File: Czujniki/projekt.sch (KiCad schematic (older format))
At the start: 44 parts, among them P1 CONN_01X08, U1 MCP1700, U10 PCA9306, U12 SHTC1, U14 LM4041, U15 MCP6231, U6 MCP3201, U7 DS1338, U8 MCP6L1, U9 MCP6L1, Y1 Crystal

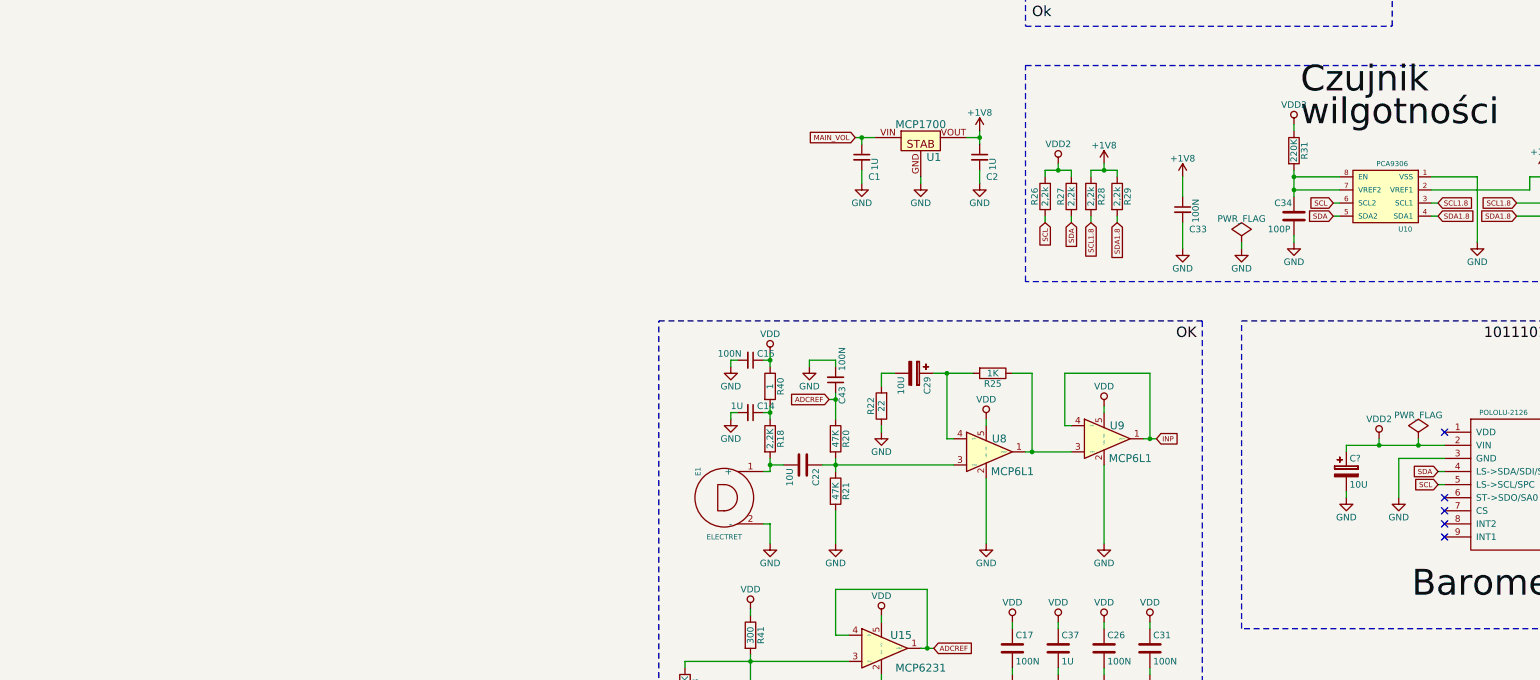
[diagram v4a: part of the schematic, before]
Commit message: Edits + additional program for dust controller
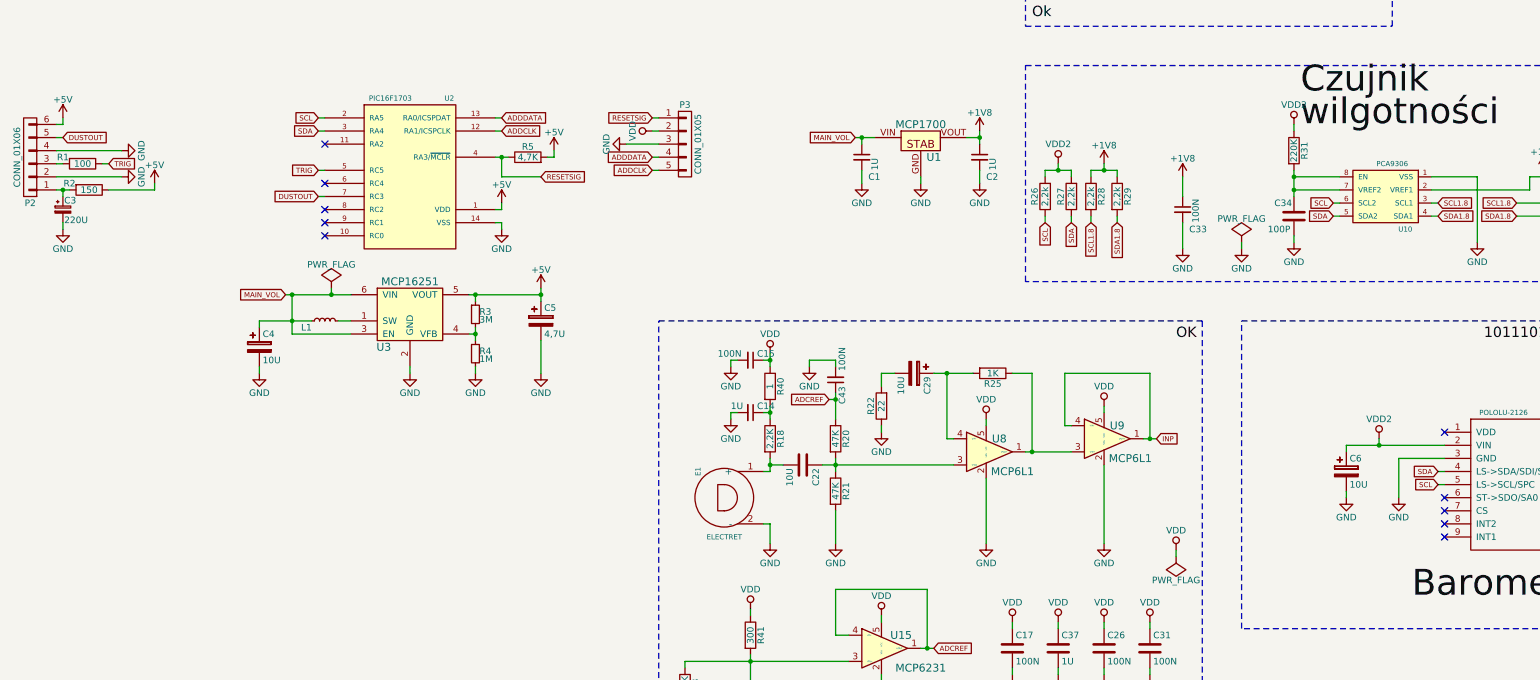
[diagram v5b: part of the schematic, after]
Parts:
- added C3: 220U, Capacitors_Tantalum_SMD:TantalC_SizeX_EIA-7343, symbol CP_Small
- added C4: 10U, Capacitors_Tantalum_SMD:TantalC_SizeX_EIA-7343, symbol CP
- added C5: 4,7U, Capacitors_Tantalum_SMD:TantalC_SizeA_EIA-3216_HandSoldering, symbol CP
- added L1: NLCV32T-4R7M-PF, SMD_Packages:SMD-1210_Pol, symbol L_Small
- added P2: CONN_01X06, Socket_Strips:Socket_Strip_Straight_1x06, symbol CONN_01X06
- added P3: CONN_01X05, Socket_Strips:Socket_Strip_Straight_1x05, symbol CONN_01X05
- added R1: 100, Resistors_SMD:R_0603, symbol R
- added R2: 150, Resistors_SMD:R_0805, symbol R
- added R3: 3M, Resistors_SMD:R_0603, symbol R_Small
- added R4: 1M, Resistors_SMD:R_0603, symbol R_Small
- added R5: 4,7K, Resistors_SMD:R_0603, symbol R
- added U2: PIC16F1703, SMD_Packages:SOIC-14_N, symbol PIC16F1703
- added U3: MCP16251, Housings_SOT-23_SOT-143_TSOT-6:SOT-23-6, symbol MCP16251
- C6: renamed from C?; footprint (none) -> SMD_Packages:SMD-1206_Pol
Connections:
- net GND: now also C3.2, C4.2, C5.2, P2.2 (P2), P2.4 (P4), P3.3 (P3), R4.2, U2.14 (VSS), U3.2 (GND)
- net MAIN_VOL: now also C4.1, L1.1, U3.3 (EN), U3.6 (VIN)
- net SCL: now also U2.2 (RA5)
- net SDA: now also U2.3 (RA4)
- net VDD: now also P3.2 (P2)
- new net: L1.2, U3.1 (SW)
- new net: R3.2, R4.1, U3.4 (VFB)
- new net: C3.1, P2.1 (P1), R2.2
- new net: P2.3 (P3), R1.2
- new net +5V: C5.1, P2.6 (P6), R2.1, R3.1, R5.2, U2.1 (VDD), U3.5 (VOUT)
- new net ADDCLK: P3.5 (P5), U2.12 (RA1/ICSPCLK)
- new net ADDDATA: P3.4 (P4), U2.13 (RA0/ICSPDAT)
- new net DUSTOUT: P2.5 (P5), U2.7 (RC3)
- new net RESETSIG: P3.1 (P1), R5.1, U2.4 (RA3/~MCLR)
- new net TRIG: R1.1, U2.5 (RC5)
- no-connect marks 6 -> 11

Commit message: Commit message
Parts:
- added R6: 10K, Resistors_SMD:R_0603, symbol R
- added R7, R8: 4,7K, Resistors_SMD:R_0603, symbol R
- added T1: Si2323DS, Footprinty:SOT23, symbol Si2323DS
- added T2, T3: FDV303N, Footprinty:SOT23, symbol FDV303N
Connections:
- net +5V: now also R7.1, R8.1, T1.S; no longer P2.6 (P6), R2.1
- net SCL: now also T3.S; no longer U2.2 (RA5)
- net SDA: now also T2.S; no longer U2.3 (RA4)
- net VDD: now also T2.G, T3.G
- net CONTROL: now reaches U2.6 (RC4)
- net CONTROL: now also R6.1
- new net: P2.6 (P6), R2.1, T1.D
- new net: R6.2, T1.G
- new net SCL5: R8.2, T2.D, U2.2 (RA5)
- new net SDA5: R7.2, T3.D, U2.3 (RA4)
- no-connect marks 11 -> 10
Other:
- moved on the sheet: C3, C4, C5, L1, P2, P3, R1, R2, R3, R4, R5, U2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

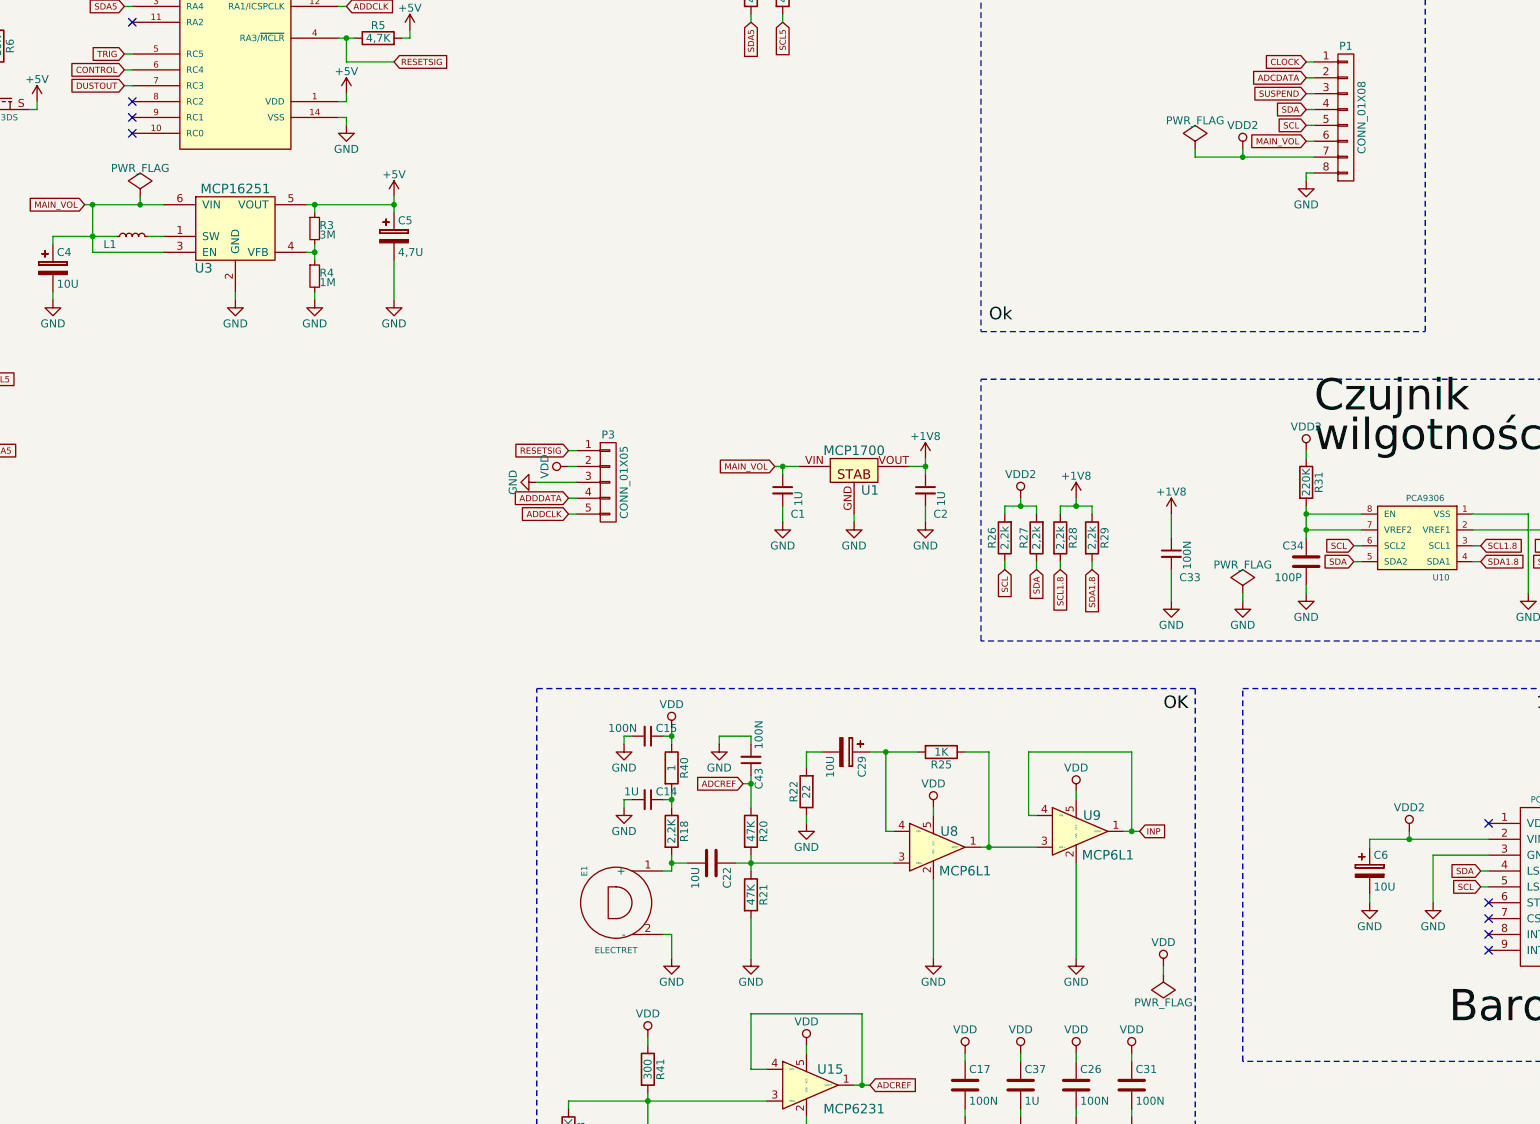
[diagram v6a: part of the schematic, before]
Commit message: Supply on sensor board done. Before gas sensor adding.
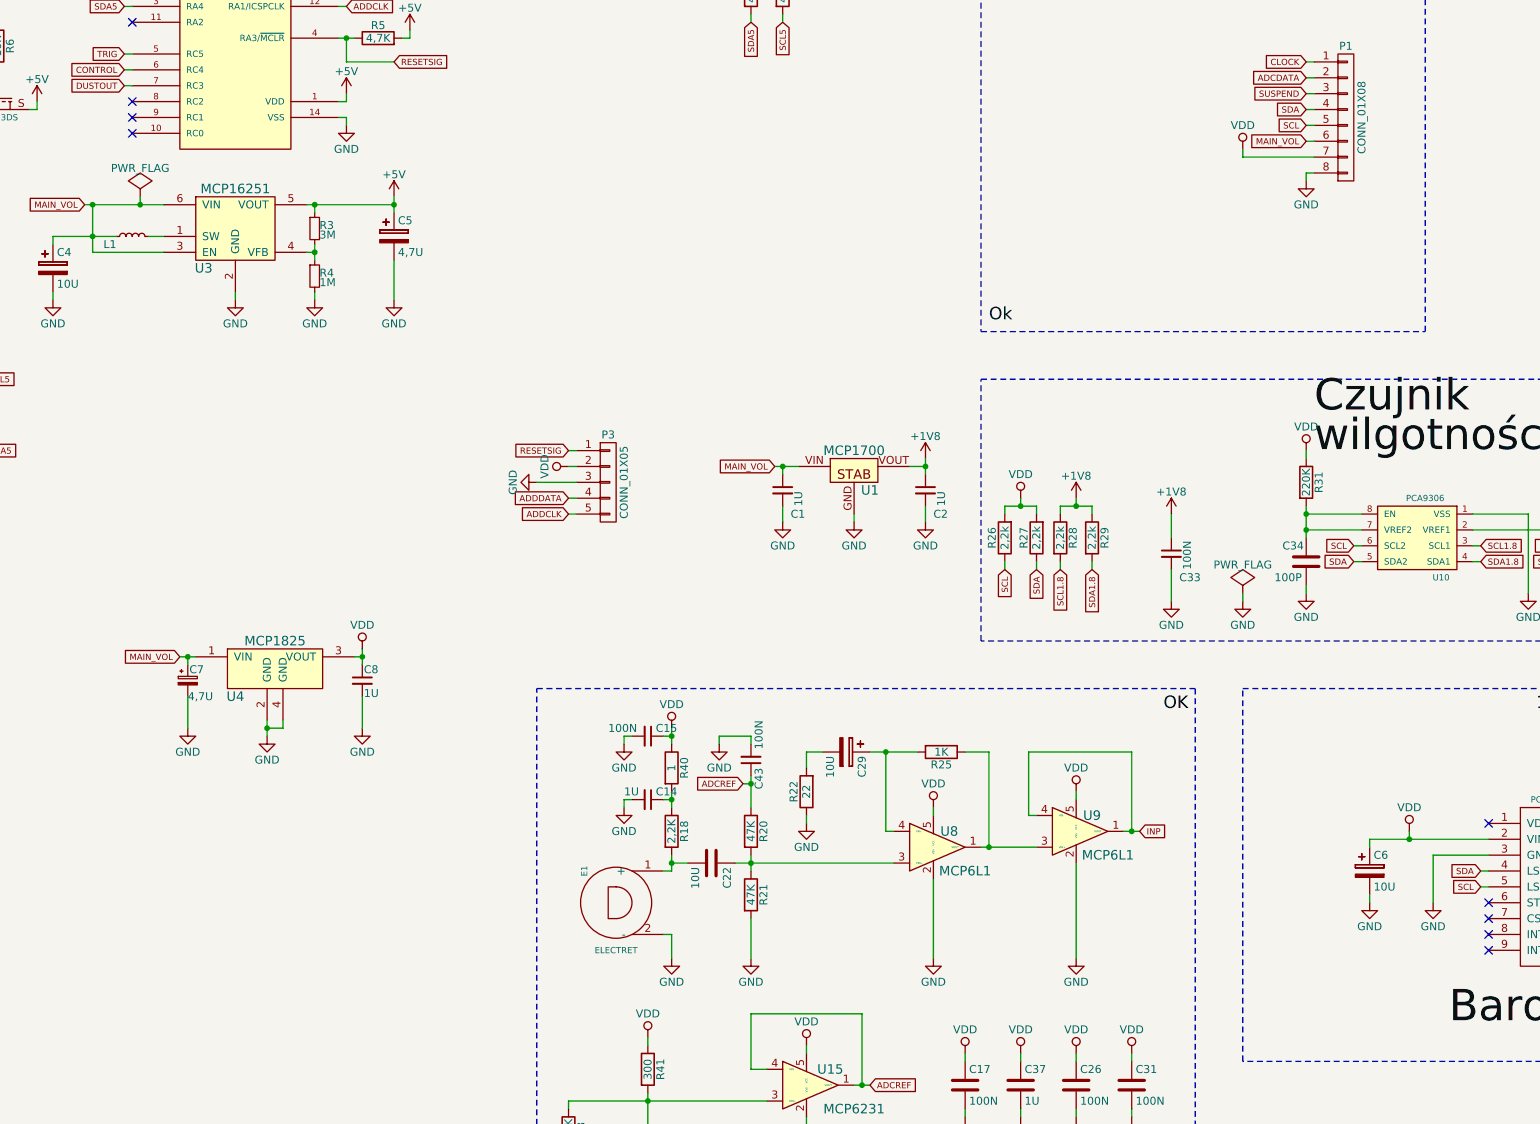
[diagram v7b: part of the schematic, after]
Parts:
- added C7: 4,7U, Capacitors_Tantalum_SMD:TantalC_SizeA_EIA-3216_HandSoldering, symbol CP_Small
- added C8: 1U, Capacitors_SMD:C_0805_HandSoldering, symbol C_Small
- added U4: MCP1825, SMD_Packages:SOT-223, symbol MCP1825
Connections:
- net VDD2 is gone; now on net VDD: C6.1, CE1.2 (VIN), P1.7 (P7), R26.2, R27.2, R31.1
- net GND: now also C7.2, C8.2, U4.2 (GND), U4.4 (GND)
- net MAIN_VOL: now also C7.1, U4.1 (VIN)
- net VDD: now also C8.1, U4.3 (VOUT)
